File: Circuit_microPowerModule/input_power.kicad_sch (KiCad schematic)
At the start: 42 parts, among them Q301 MMBT3906, Q302 RK7002BM, Q303 IRF5305S, SW302 SW_DPDT_x2, U7 MP2315S

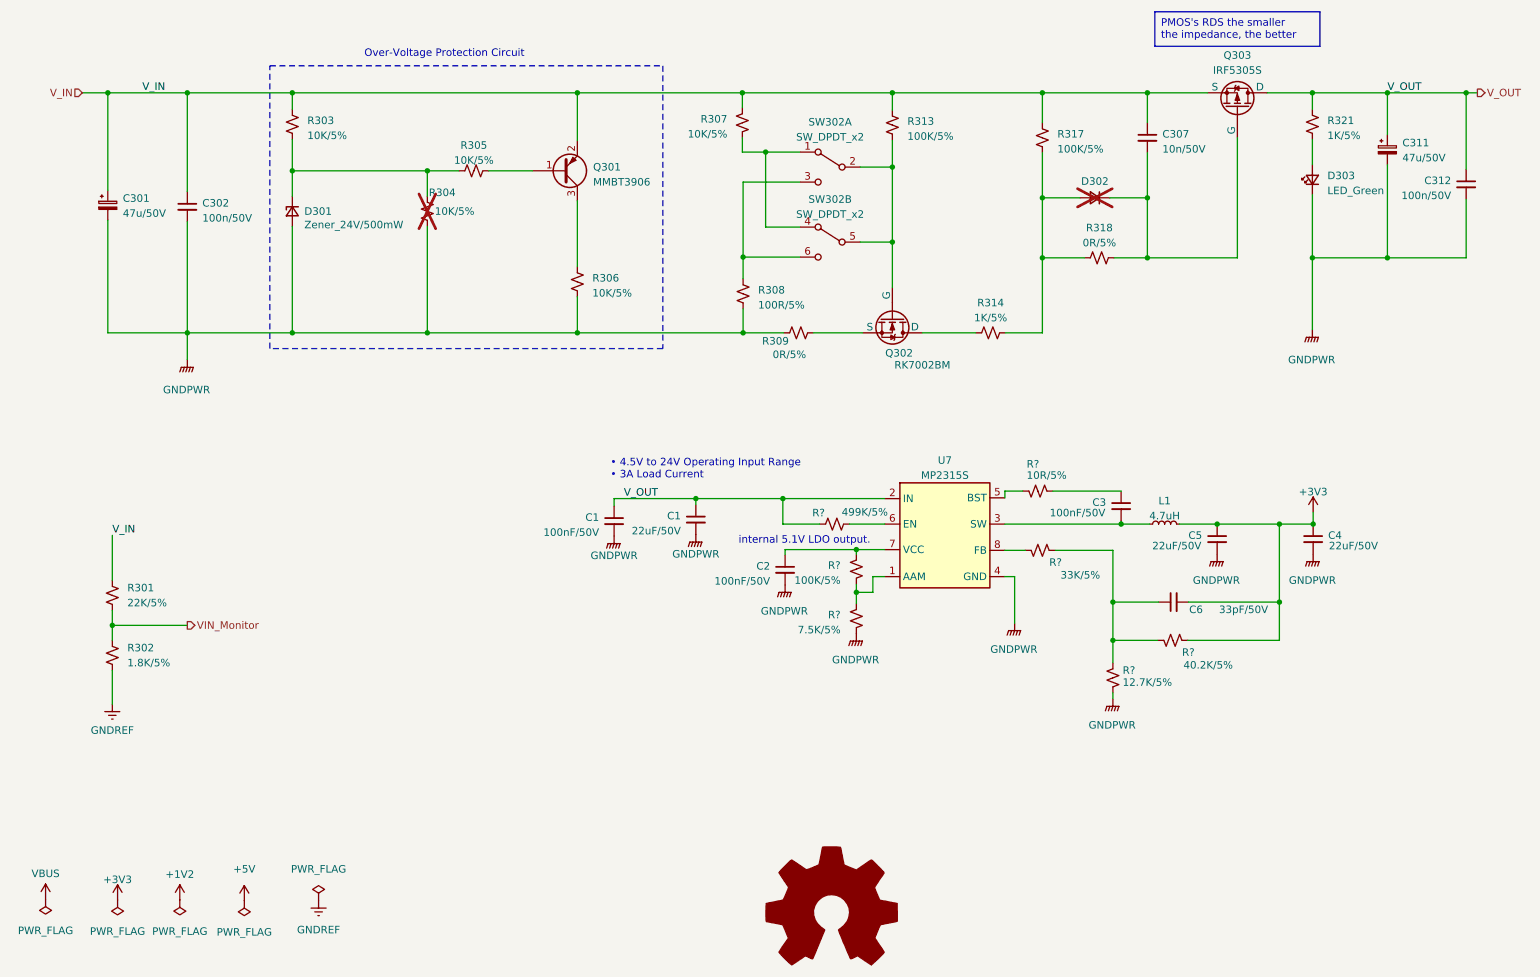
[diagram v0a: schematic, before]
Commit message: modify ERC error, protect components
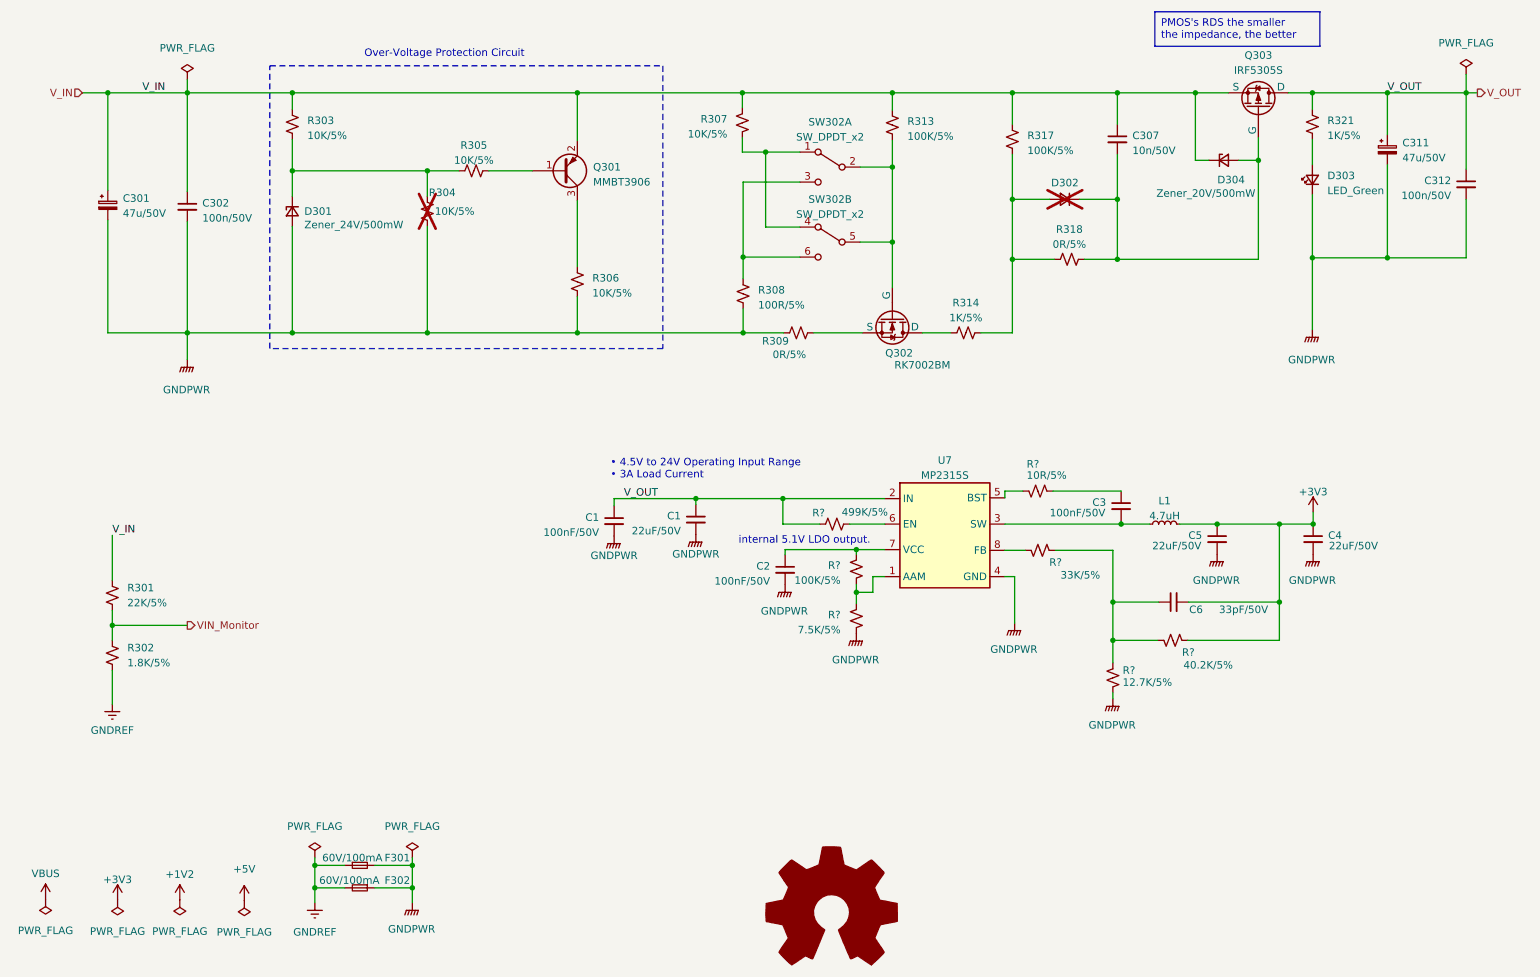
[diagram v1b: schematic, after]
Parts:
- added D304: Zener_20V/500mW, Diode_SMD:D_SOD-123, symbol Device:D_Zener_Small
- added F301, F302: 60V/100mA, Fuse:Fuse_1206_3216Metric, symbol Device:Fuse_Small
- SW302: footprint Button_Switch_THT:SW_Push_2P2T_Toggle_CK_PVA2xxH1xxxxxxV2 -> micro-PowerModule_Library:SW_DIP_5176_SPDT
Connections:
- net GNDPWR: now also F301.2, F302.1
- net GNDREF: now also F301.1, F302.2
- net V_IN: now also D304.1 (K)
- net at C307.2, D302.1 (K), Q303.2 (G)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: now also D304.2 (A)
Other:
- title: (none) -> µPower Module
- moved on the sheet: C307, D302, Q303, R314, R317, R318

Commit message: modify ERC warning
modify OPA, TVS-Diode, Cap
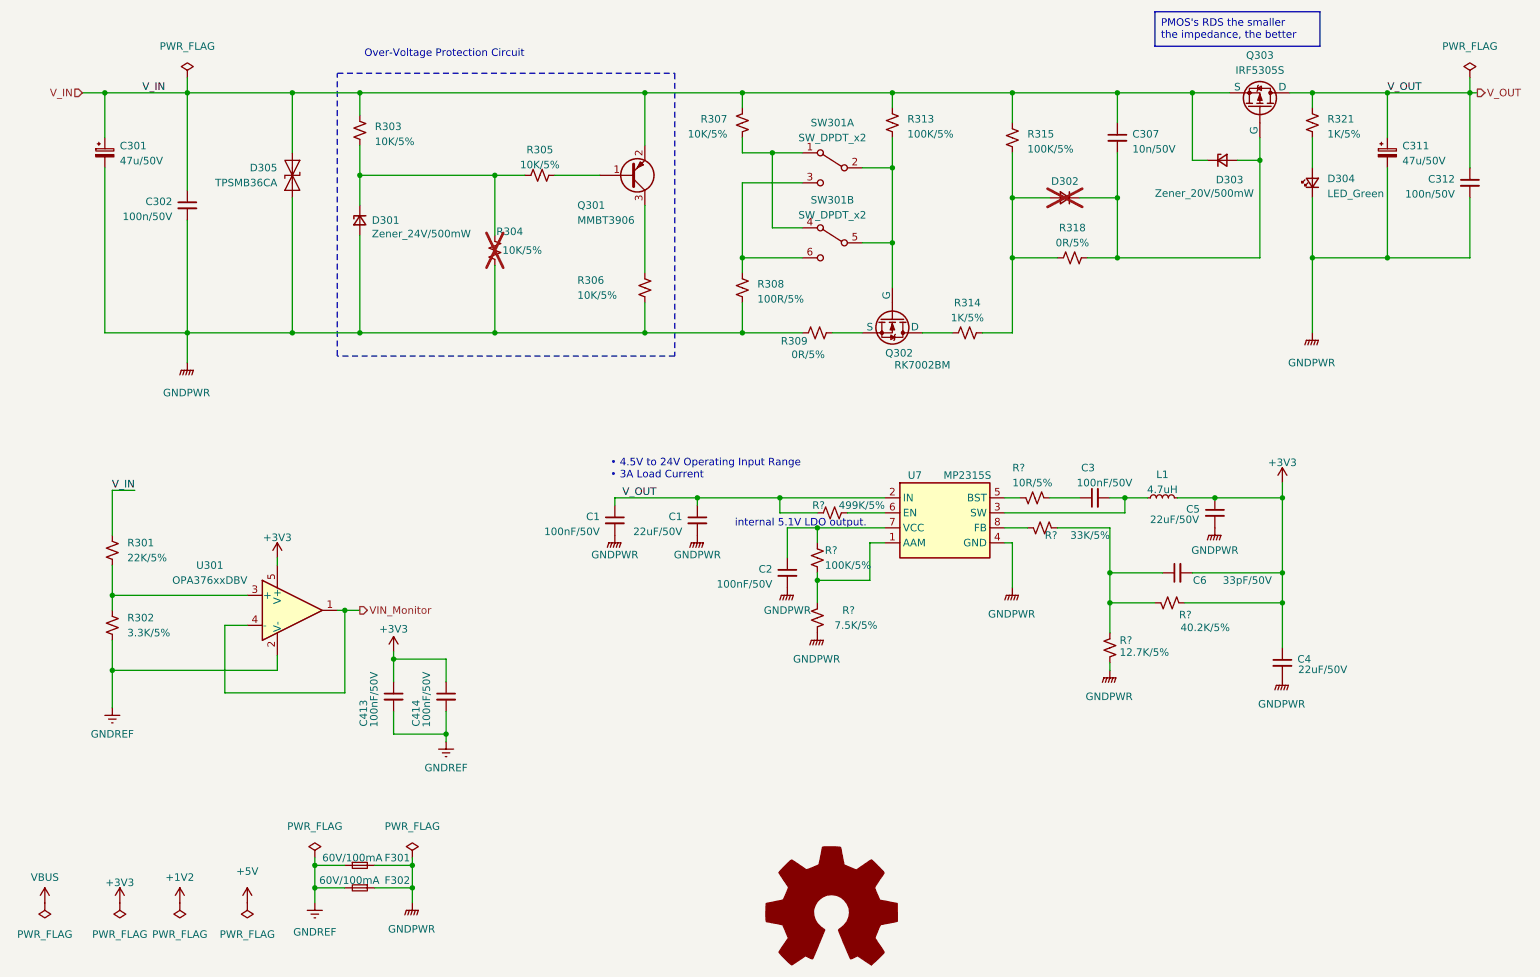
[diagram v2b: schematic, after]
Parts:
- added C413, C414: 100nF/50V, Capacitor_SMD:C_0603_1608Metric, symbol Device:C_Small
- added D305: TPSMB36CA, Diode_SMD:D_SMB, symbol Diode:ESD131-B1-W0201
- added U301: OPA376xxDBV, Package_TO_SOT_SMD:SOT-23-5, symbol Amplifier_Operational:OPA376xxDBV
- C1, C301, C311, C4, C5: footprint (none) -> Capacitor_SMD:C_1206_3216Metric
- R302: value 1.8K/5% -> 3.3K/5%
- renumbered D304 to D303, D303 to D304, R317 to R315, SW302 to SW301
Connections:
- net +3V3: now also C413.1, C414.1, U301.5 (V+)
- net GNDPWR: now also D305.1 (A1)
- net GNDREF: now also C413.2, C414.2, U301.2 (V-)
- net VIN_Monitor: now also U301.1, U301.4 (-); no longer R301.2, R302.1
- net V_IN: now also D305.2 (A2)
- new net: R301.2, R302.1, U301.3 (+)
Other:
- moved on the sheet: C2, C3, C301, C311, C312, C4, C5, C6, D301, D304, L1, Q301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

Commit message: update system power circuit layout
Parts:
- C4, C5: footprint Capacitor_SMD:C_1206_3216Metric -> Capacitor_SMD:C_1210_3225Metric
- L1: footprint Inductor_SMD_Wurth:L_Wurth_WE-LQSH-2512 -> Inductor_SMD:L_Sunlord_MWSA1204S-4R7
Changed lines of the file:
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@@
       (effects (font (size 1.27 1.27)) (justify left))
     )
-    (property "Footprint" "Capacitor_SMD:C_1206_3216Metric" (at 224.79 109.22 0)
+    (property "Footprint" "Capacitor_SMD:C_1210_3225Metric" (at 224.79 109.22 0)
       (effects (font (size 1.27 1.27)) hide)
     )
@@
       (effects (font (size 1.27 1.27)))
     )
-    (property "Footprint" "Inductor_SMD_Wurth:L_Wurth_WE-LQSH-2512" (at 215.9 106.68 0)
+    (property "Footprint" "Inductor_SMD:L_Sunlord_MWSA1204S-4R7" (at 215.9 106.68 0)
       (effects (font (size 1.27 1.27)) hide)
     )
@@
       (effects (font (size 1.27 1.27)) (justify left))
     )
-    (property "Footprint" "Capacitor_SMD:C_1206_3216Metric" (at 236.22 134.62 0)
-      (effects (font (size 1.27 1.27)) hide)
-    )
+    (property "Footprint" "Capacitor_SMD:C_1210_3225Metric" (at 236.22 134.62 0)
+      (effects (font (size 1.27 1.27)) hide)
+    )
